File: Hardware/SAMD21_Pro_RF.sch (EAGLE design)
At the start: 70 parts, among them J12 JST, J13 U.FL, J7 PTH, J9 External On/Off, Q1 2.5A/30V, U1 MCP73831, U3 RFM95W, U4 ATSAMD21G, U6 3.3V, Y1 32.768kHz

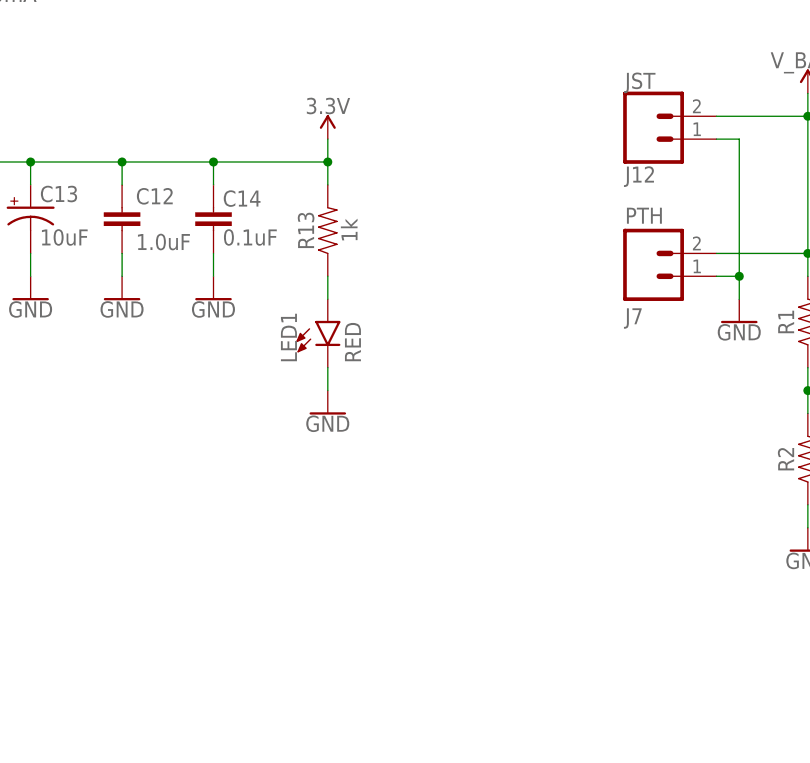
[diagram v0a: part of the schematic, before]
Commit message: Added LED disable Jumper NC trace
for easier access to disable Power LED in  low power applications
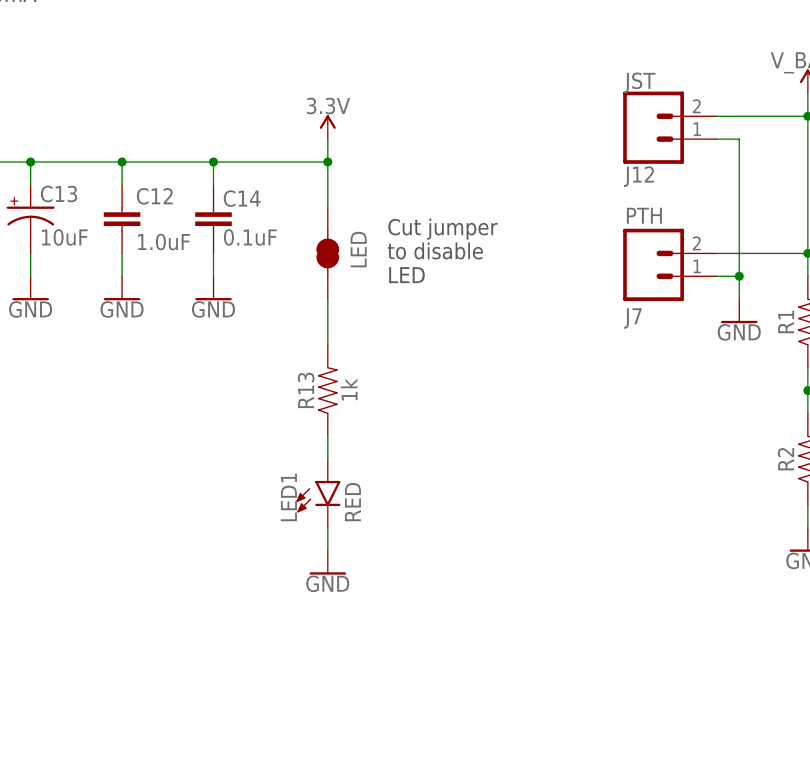
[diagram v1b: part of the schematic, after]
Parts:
- added LED: JUMPER-SMT_2_NC_TRACE_SILK, SparkFun-Jumpers:JUMPER-SMT_2_NC_TRACE_SILK
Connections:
- new net N$5: LED.2, R13.2
- net 3.3V: now also LED.1; no longer R13.2
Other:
- note added: "Cut jumper to disable LED"
- moved on the sheet: LED1, R13
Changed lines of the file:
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@@
 <part name="J10" library="SparkFun-Connectors" deviceset="CONN_01" device="PTH_NO_SILK_YES_STOP"/>
 <part name="J14" library="SparkFun-Connectors" deviceset="CONN_01" device="PTH_NO_SILK_YES_STOP"/>
+<part name="LED" library="SparkFun-Jumpers" deviceset="JUMPER-SMT_2_NC_TRACE" device="_SILK" package3d_urn="urn:adsk.eagle:package:39281/1" value=""/>
 </parts>
 <sheets>
@@
 <text x="331.978" y="7.112" size="2.54" layer="94" font="vector">Revised by:</text>
 <text x="357.378" y="7.112" size="2.54" layer="94" font="vector">Pete Lewis</text>
+<text x="346.964" y="207.518" size="1.778" layer="97" font="vector">Cut jumper
+to disable
+LED</text>
 </plain>
 <instances>
@@
 <attribute name="VALUE" x="317.5" y="205.486" size="1.778" layer="96" align="top-center"/>
 </instance>
-<instance part="R13" gate="G$1" x="340.36" y="213.36" smashed="yes" rot="R90">
-<attribute name="NAME" x="338.836" y="213.36" size="1.778" layer="95" font="vector" rot="R90" align="bottom-center"/>
-<attribute name="VALUE" x="341.884" y="213.36" size="1.778" layer="96" font="vector" rot="R90" align="top-center"/>
-</instance>
-<instance part="LED1" gate="G$1" x="340.36" y="203.2" smashed="yes">
-<attribute name="NAME" x="336.931" y="198.628" size="1.778" layer="95" font="vector" rot="R90"/>
-<attribute name="VALUE" x="342.265" y="198.628" size="1.778" layer="96" font="vector" rot="R90" align="top-left"/>
-</instance>
-<instance part="GND31" gate="1" x="340.36" y="193.04" smashed="yes">
-<attribute name="VALUE" x="340.36" y="192.786" size="1.778" layer="96" align="top-center"/>
+<instance part="R13" gate="G$1" x="340.36" y="195.58" smashed="yes" rot="R90">
+<attribute name="NAME" x="338.836" y="195.58" size="1.778" layer="95" font="vector" rot="R90" align="bottom-center"/>
+<attribute name="VALUE" x="341.884" y="195.58" size="1.778" layer="96" font="vector" rot="R90" align="top-center"/>
+</instance>
+<instance part="LED1" gate="G$1" x="340.36" y="185.42" smashed="yes">
+<attribute name="NAME" x="336.931" y="180.848" size="1.778" layer="95" font="vector" rot="R90"/>
+<attribute name="VALUE" x="342.265" y="180.848" size="1.778" layer="96" font="vector" rot="R90" align="top-left"/>
+</instance>
+<instance part="GND31" gate="1" x="340.36" y="175.26" smashed="yes">
+<attribute name="VALUE" x="340.36" y="175.006" size="1.778" layer="96" align="top-center"/>
 </instance>
 <instance part="C14" gate="G$1" x="327.66" y="215.9" smashed="yes" rot="R180">
@@
 <attribute name="VALUE" x="416.56" y="70.866" size="1.778" layer="96" font="vector" rot="R180"/>
 <attribute name="NAME" x="416.56" y="62.992" size="1.778" layer="95" font="vector" rot="R180"/>
+</instance>
+<instance part="LED" gate="G$1" x="340.36" y="210.82" smashed="yes" rot="R270">
+<attribute name="NAME" x="342.9" y="213.36" size="1.778" layer="95" font="vector" rot="R270"/>
+<attribute name="VALUE" x="337.82" y="213.36" size="1.778" layer="96" font="vector" rot="R270" align="top-left"/>
 </instance>
 </instances>
@@
 </segment>
 <segment>
-<wire x1="340.36" y1="195.58" x2="340.36" y2="198.12" width="0.1524" layer="91"/>
+<wire x1="340.36" y1="177.8" x2="340.36" y2="180.34" width="0.1524" layer="91"/>
 <pinref part="LED1" gate="G$1" pin="C"/>
 <pinref part="GND31" gate="1" pin="GND"/>
@@
 <wire x1="327.66" y1="220.98" x2="340.36" y2="220.98" width="0.1524" layer="91"/>
 <wire x1="340.36" y1="220.98" x2="340.36" y2="223.52" width="0.1524" layer="91"/>
-<wire x1="340.36" y1="220.98" x2="340.36" y2="218.44" width="0.1524" layer="91"/>
 <wire x1="317.5" y1="220.98" x2="317.5" y2="218.44" width="0.1524" layer="91"/>
 <wire x1="307.34" y1="220.98" x2="307.34" y2="218.44" width="0.1524" layer="91"/>
 <wire x1="327.66" y1="218.44" x2="327.66" y2="220.98" width="0.1524" layer="91"/>
-<junction x="340.36" y="220.98"/>
 <junction x="317.5" y="220.98"/>
 <junction x="307.34" y="220.98"/>
 <junction x="327.66" y="220.98"/>
 <pinref part="U6" gate="G$1" pin="OUT"/>
-<pinref part="R13" gate="G$1" pin="2"/>
 <pinref part="C12" gate="G$1" pin="1"/>
 <pinref part="C13" gate="G$1" pin="+"/>
 <pinref part="C14" gate="G$1" pin="2"/>
 <pinref part="P+10" gate="G$1" pin="3.3V"/>
+<pinref part="LED" gate="G$1" pin="1"/>
+<wire x1="340.36" y1="220.98" x2="340.36" y2="215.9" width="0.1524" layer="91"/>
+<junction x="340.36" y="220.98"/>
 </segment>
 <segment>
@@
 <net name="N$38" class="0">
 <segment>
-<wire x1="340.36" y1="205.74" x2="340.36" y2="208.28" width="0.1524" layer="91"/>
+<wire x1="340.36" y1="187.96" x2="340.36" y2="190.5" width="0.1524" layer="91"/>
 <pinref part="R13" gate="G$1" pin="1"/>
 <pinref part="LED1" gate="G$1" pin="A"/>
@@
 </segment>
 </net>
+<net name="N$5" class="0">
+<segment>
+<pinref part="LED" gate="G$1" pin="2"/>
+<pinref part="R13" gate="G$1" pin="2"/>
+<wire x1="340.36" y1="205.74" x2="340.36" y2="200.66" width="0.1524" layer="91"/>
+</segment>
+</net>
 </nets>
 </sheet>
@@
 will not be understood (or retained) with this version.
 </note>
+<note version="8.3" severity="warning">
+Since Version 8.3, EAGLE supports the association of 3D packages
+with devices in libraries, schematics, and board files. Those 3D
+packages will not be understood (or retained) with this version.
+</note>
 </compatibility>

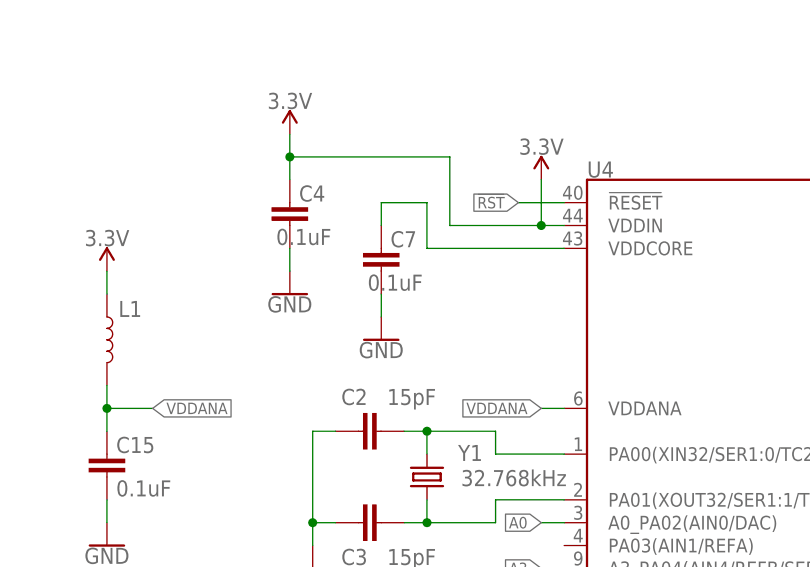
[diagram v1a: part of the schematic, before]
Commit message: Changed C7 to 1.0uF as recommended in DS
This is the VDDCORE cap to GND.
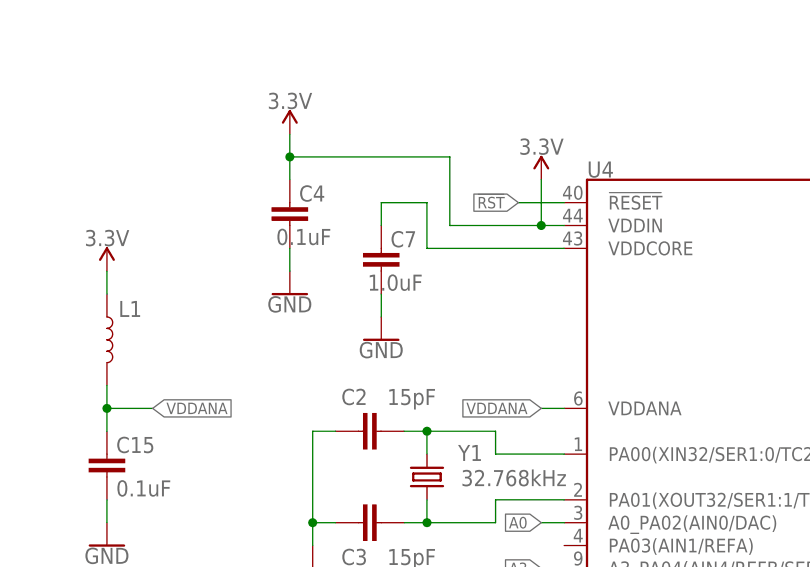
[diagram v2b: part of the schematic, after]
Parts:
- C7: value 0.1uF -> 1.0uF; device SparkFun-Capacitors:0.1UF-0603-25V-(+80/-20%) -> SparkFun-Capacitors:1.0UF-0603-16V-10%
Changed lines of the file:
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@@
 <part name="GND8" library="SparkFun-PowerSymbols" deviceset="GND" device=""/>
 <part name="SUPPLY1" library="SparkFun-PowerSymbols" deviceset="VIN" device=""/>
-<part name="C7" library="SparkFun-Capacitors" deviceset="0.1UF" device="-0603-25V-(+80/-20%)" value="0.1uF"/>
+<part name="C7" library="SparkFun-Capacitors" deviceset="1.0UF" device="-0603-16V-10%" value="1.0uF"/>
 <part name="GND19" library="SparkFun-PowerSymbols" deviceset="GND" device=""/>
 <part name="LOGO3" library="SparkFun-Aesthetics" deviceset="QWIIC_LOGO" device="_5MM"/>

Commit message: sch stuff
- removed one extra 3.3V symbol near IC
- added vcc range to sch near IC
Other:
- note added: "VCC RANGE: 1.62-3.63V"
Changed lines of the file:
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@@
 <part name="L1" library="SparkFun-Coils" deviceset="INDUCTOR" device="FB-30OHM"/>
 <part name="P+8" library="SparkFun-PowerSymbols" deviceset="3.3V" device=""/>
-<part name="P+11" library="SparkFun-PowerSymbols" deviceset="3.3V" device=""/>
 <part name="C10" library="SparkFun-Capacitors" deviceset="0.1UF" device="-0603-25V-(+80/-20%)" value="0.1uF"/>
 <part name="GND13" library="SparkFun-PowerSymbols" deviceset="GND" device=""/>
@@
 to disable
 LED</text>
+<text x="88.9" y="152.4" size="2.54" layer="97" font="vector">VCC RANGE: 1.62-3.63V</text>
 </plain>
 <instances>
@@
 <instance part="P+8" gate="G$1" x="12.7" y="127" smashed="yes">
 <attribute name="VALUE" x="12.7" y="129.794" size="1.778" layer="96" align="bottom-center"/>
-</instance>
-<instance part="P+11" gate="G$1" x="73.66" y="243.84" smashed="yes">
-<attribute name="VALUE" x="73.66" y="246.634" size="1.778" layer="96" align="bottom-center"/>
 </instance>
 <instance part="C10" gate="G$1" x="157.48" y="233.68" smashed="yes" rot="R180">
@@
 <junction x="45.72" y="246.38"/>
 <wire x1="63.5" y1="246.38" x2="63.5" y2="238.76" width="0.1524" layer="91"/>
-<wire x1="76.2" y1="238.76" x2="73.66" y2="238.76" width="0.1524" layer="91"/>
-<wire x1="73.66" y1="238.76" x2="73.66" y2="243.84" width="0.1524" layer="91"/>
-<pinref part="P+11" gate="G$1" pin="3.3V"/>
-<junction x="73.66" y="238.76"/>
 <pinref part="U4" gate="G$1" pin="VDDIN"/>
-<wire x1="73.66" y1="238.76" x2="63.5" y2="238.76" width="0.1524" layer="91"/>
-</segment>
-<segment>
+<wire x1="76.2" y1="238.76" x2="63.5" y2="238.76" width="0.1524" layer="91"/>
+</segment>
+<segment>
